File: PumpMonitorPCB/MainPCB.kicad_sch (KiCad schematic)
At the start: 2 parts, among them J1 Mains terminals, J2 Mains terminals

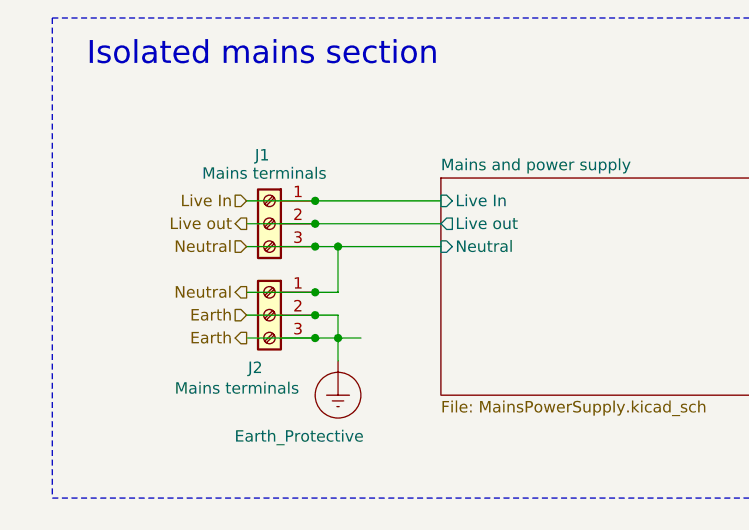
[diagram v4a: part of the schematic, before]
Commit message: Swapped current measurement to neutral (wiring diagram needs updating).
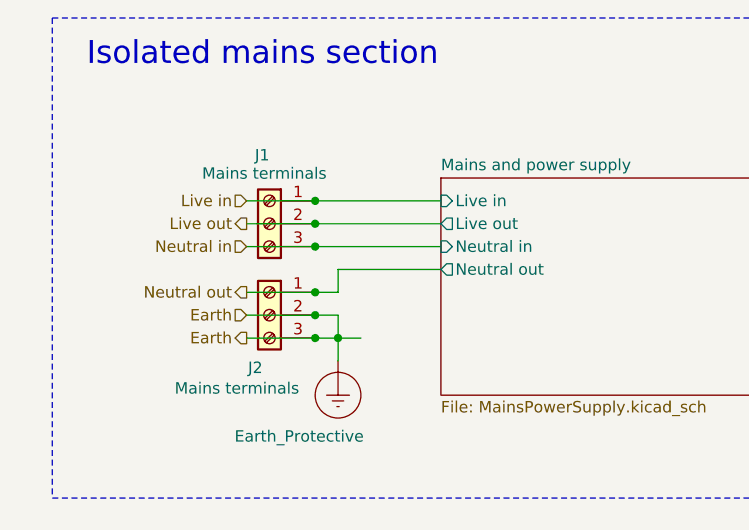
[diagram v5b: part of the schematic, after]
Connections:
- net Live In renamed Live in
- net Neutral renamed Neutral in
- net Neutral in: no longer J2.1 (Pin_1)
- new net Neutral out: J2.1 (Pin_1)
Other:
- sheet Mains and power supply ports: added Live in, Neutral in, Neutral out; removed Live In, Neutral
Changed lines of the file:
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@@
-	)
-	(junction
-		(at 68.58 53.34)
-		(diameter 0)
-		(color 0 0 0 0)
 	)
 	(junction
@@
 		)
 	)
-	(wire
-		(pts
-			(xy 66.04 58.42) (xy 68.58 58.42)
-		)
-		(stroke
-			(width 0)
-			(type default)
-		)
-	)
 	(bus
 		(pts
@@
 		(pts
 			(xy 68.58 63.5) (xy 71.12 63.5)
+		)
+		(stroke
+			(width 0)
+			(type default)
+		)
+	)
+	(wire
+		(pts
+			(xy 68.58 55.88) (xy 68.58 58.42)
 		)
 		(stroke
@@
 	(wire
 		(pts
-			(xy 66.04 53.34) (xy 68.58 53.34)
+			(xy 66.04 53.34) (xy 80.01 53.34)
 		)
 		(stroke
@@
 	(wire
 		(pts
-			(xy 68.58 53.34) (xy 80.01 53.34)
-		)
-		(stroke
-			(width 0)
-			(type default)
-		)
-	)
-	(wire
-		(pts
 			(xy 153.67 59.69) (xy 181.61 59.69)
 		)
@@
 		)
 	)
+	(wire
+		(pts
+			(xy 68.58 58.42) (xy 66.04 58.42)
+		)
+		(stroke
+			(width 0)
+			(type default)
+		)
+	)
 	(bus
 		(pts
@@
 		)
 	)
-	(wire
-		(pts
-			(xy 68.58 53.34) (xy 68.58 58.42)
-		)
-		(stroke
-			(width 0)
-			(type default)
-		)
-	)
 	(bus
 		(pts
@@
 		(pts
 			(xy 66.04 60.96) (xy 68.58 60.96)
+		)
+		(stroke
+			(width 0)
+			(type default)
+		)
+	)
+	(wire
+		(pts
+			(xy 80.01 55.88) (xy 68.58 55.88)
 		)
 		(stroke
@@
 		)
 	)
-	(hierarchical_label "Live In"
+	(hierarchical_label "Live in"
 		(shape input)
 		(at 58.42 48.26 180)
@@
 		)
 	)
-	(hierarchical_label "Neutral"
+	(hierarchical_label "Neutral out"
 		(shape output)
 		(at 58.42 58.42 180)
@@
 		)
 	)
-	(hierarchical_label "Neutral"
+	(hierarchical_label "Neutral in"
 		(shape input)
 		(at 58.42 53.34 180)
@@
 			)
 		)
-		(pin "Live In" input
+		(pin "Live in" input
 			(at 80.01 48.26 180)
-			(effects
-				(font
-					(size 1.27 1.27)
-				)
-				(justify left)
-			)
-		)
-		(pin "Neutral" input
-			(at 80.01 53.34 180)
 			(effects
 				(font
@@
 			)
 		)
+		(pin "Neutral in" input
+			(at 80.01 53.34 180)
+			(effects
+				(font
+					(size 1.27 1.27)
+				)
+				(justify left)
+			)
+		)
+		(pin "Neutral out" output
+			(at 80.01 55.88 180)
+			(effects
+				(font
+					(size 1.27 1.27)
+				)
+				(justify left)
+			)
+		)

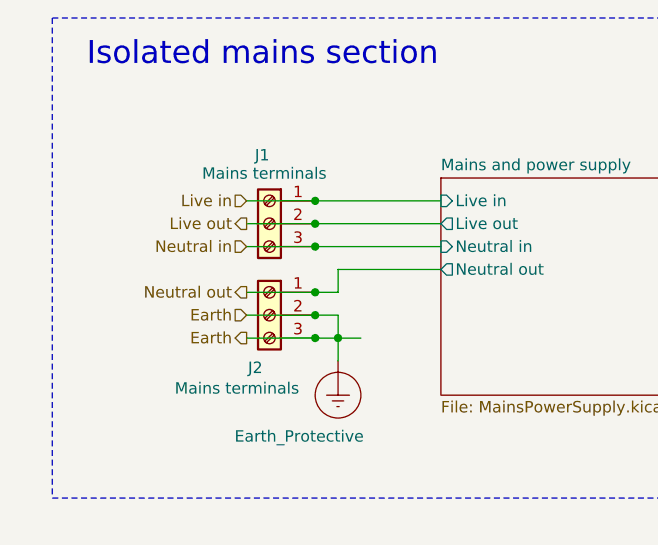
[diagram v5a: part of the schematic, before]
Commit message: Made smaller mains connector symbols, added multiple options to wiring diagram,
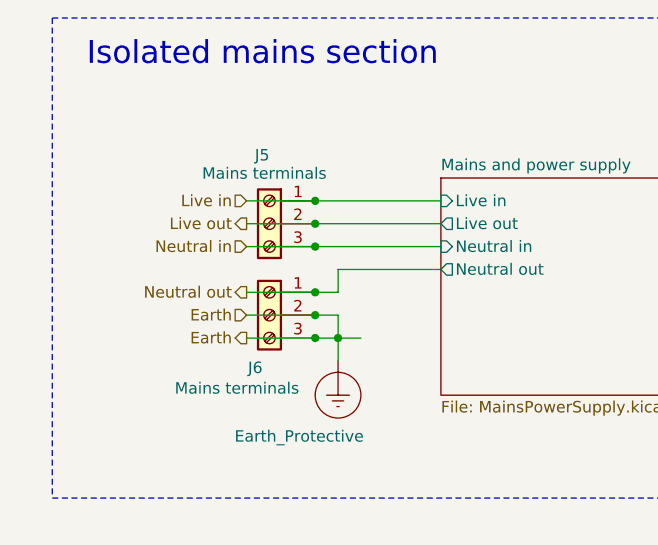
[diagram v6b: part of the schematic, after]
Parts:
- renumbered J1 to J5, J2 to J6
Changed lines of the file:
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@@
 		(on_board yes)
 		(dnp no)
-		(property "Reference" "J1"
+		(property "Reference" "J5"
 			(at 60.96 43.18 0)
 			(effects
@@
 		)
 		(pin "2"
-		)
-		(instances
-			(project ""
-				(path "/c90c4964-ca1b-44d9-8ea9-8989903af0f2/519408a1-89cc-4bd2-9b7b-cb03d2ff4d33"
-					(reference "J1")
-					(unit 1)
-				)
-			)
 		)
 	)
@@
 		(on_board yes)
 		(dnp no)
-		(property "Reference" "J2"
+		(property "Reference" "J6"
 			(at 60.198 66.802 0)
 			(effects
@@
 		(pin "2"
 		)
-		(instances
-			(project ""
-				(path "/c90c4964-ca1b-44d9-8ea9-8989903af0f2/519408a1-89cc-4bd2-9b7b-cb03d2ff4d33"
-					(reference "J2")
-					(unit 1)
-				)
-			)
-		)
 	)

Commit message: Added terminals footprint and 3D model.
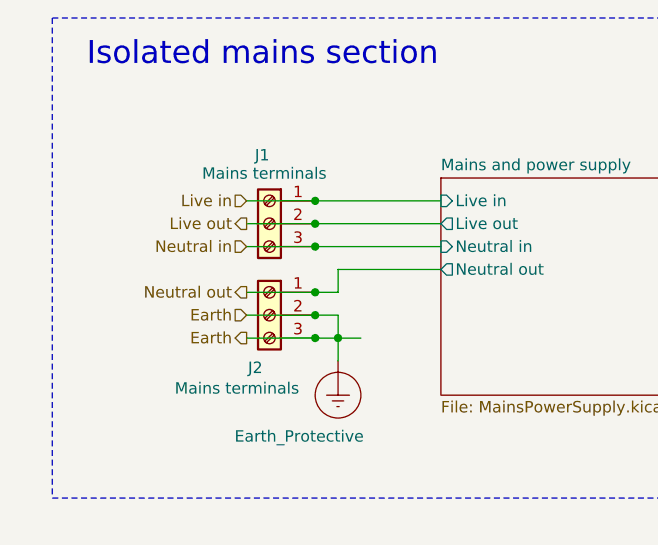
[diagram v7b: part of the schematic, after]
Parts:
- J1: renamed from J5; footprint (none) -> PumpMonitorCustomFootprints:8.25mm_ScrewTerminals
- J2: renamed from J6; footprint (none) -> PumpMonitorCustomFootprints:8.25mm_ScrewTerminals
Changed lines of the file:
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@@
 		(on_board yes)
 		(dnp no)
-		(property "Reference" "J5"
+		(property "Reference" "J1"
 			(at 60.96 43.18 0)
 			(effects
@@
 			)
 		)
-		(property "Footprint" ""
+		(property "Footprint" "PumpMonitorCustomFootprints:8.25mm_ScrewTerminals"
 			(at 60.96 50.8 0)
 			(effects
@@
 		)
 		(pin "2"
+		)
+		(instances
+			(project "PumpMonitorPCB"
+				(path "/c90c4964-ca1b-44d9-8ea9-8989903af0f2/519408a1-89cc-4bd2-9b7b-cb03d2ff4d33"
+					(reference "J1")
+					(unit 1)
+				)
+			)
 		)
 	)
@@
 		(on_board yes)
 		(dnp no)
-		(property "Reference" "J6"
+		(property "Reference" "J2"
 			(at 60.198 66.802 0)
 			(effects
@@
 			)
 		)
-		(property "Footprint" ""
+		(property "Footprint" "PumpMonitorCustomFootprints:8.25mm_ScrewTerminals"
 			(at 60.96 60.96 0)
 			(effects
@@
 		(pin "2"
 		)
+		(instances
+			(project "PumpMonitorPCB"
+				(path "/c90c4964-ca1b-44d9-8ea9-8989903af0f2/519408a1-89cc-4bd2-9b7b-cb03d2ff4d33"
+					(reference "J2")
+					(unit 1)
+				)
+			)
+		)
 	)

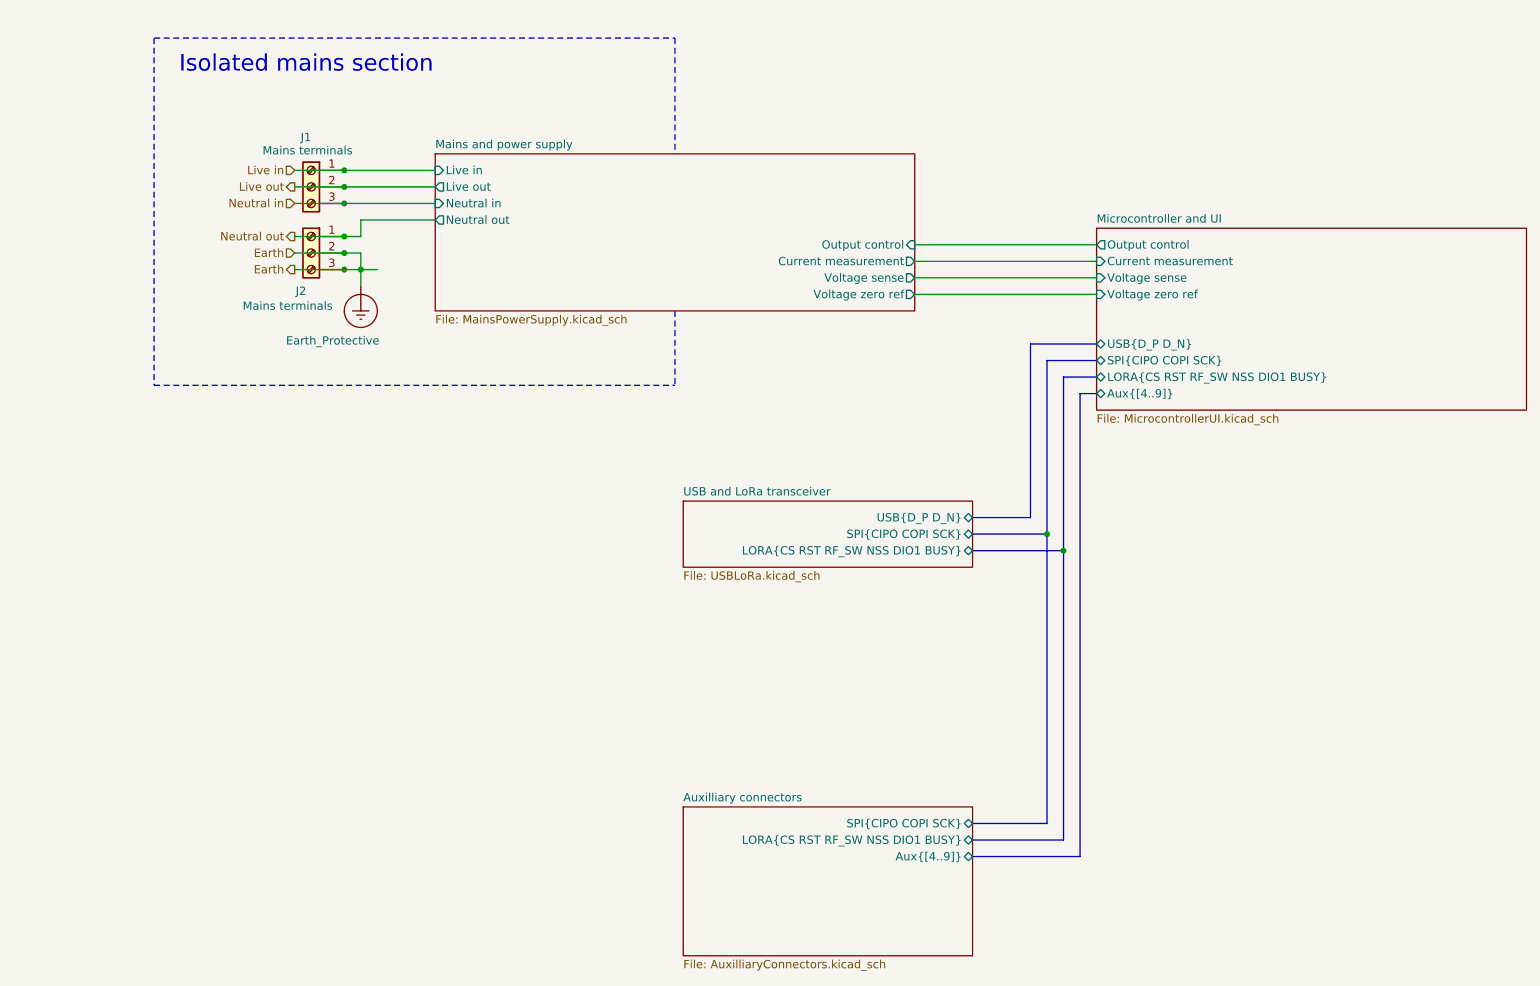
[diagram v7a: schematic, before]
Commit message: Rejigged auxilliary connectors, experimetning with kiclearance.
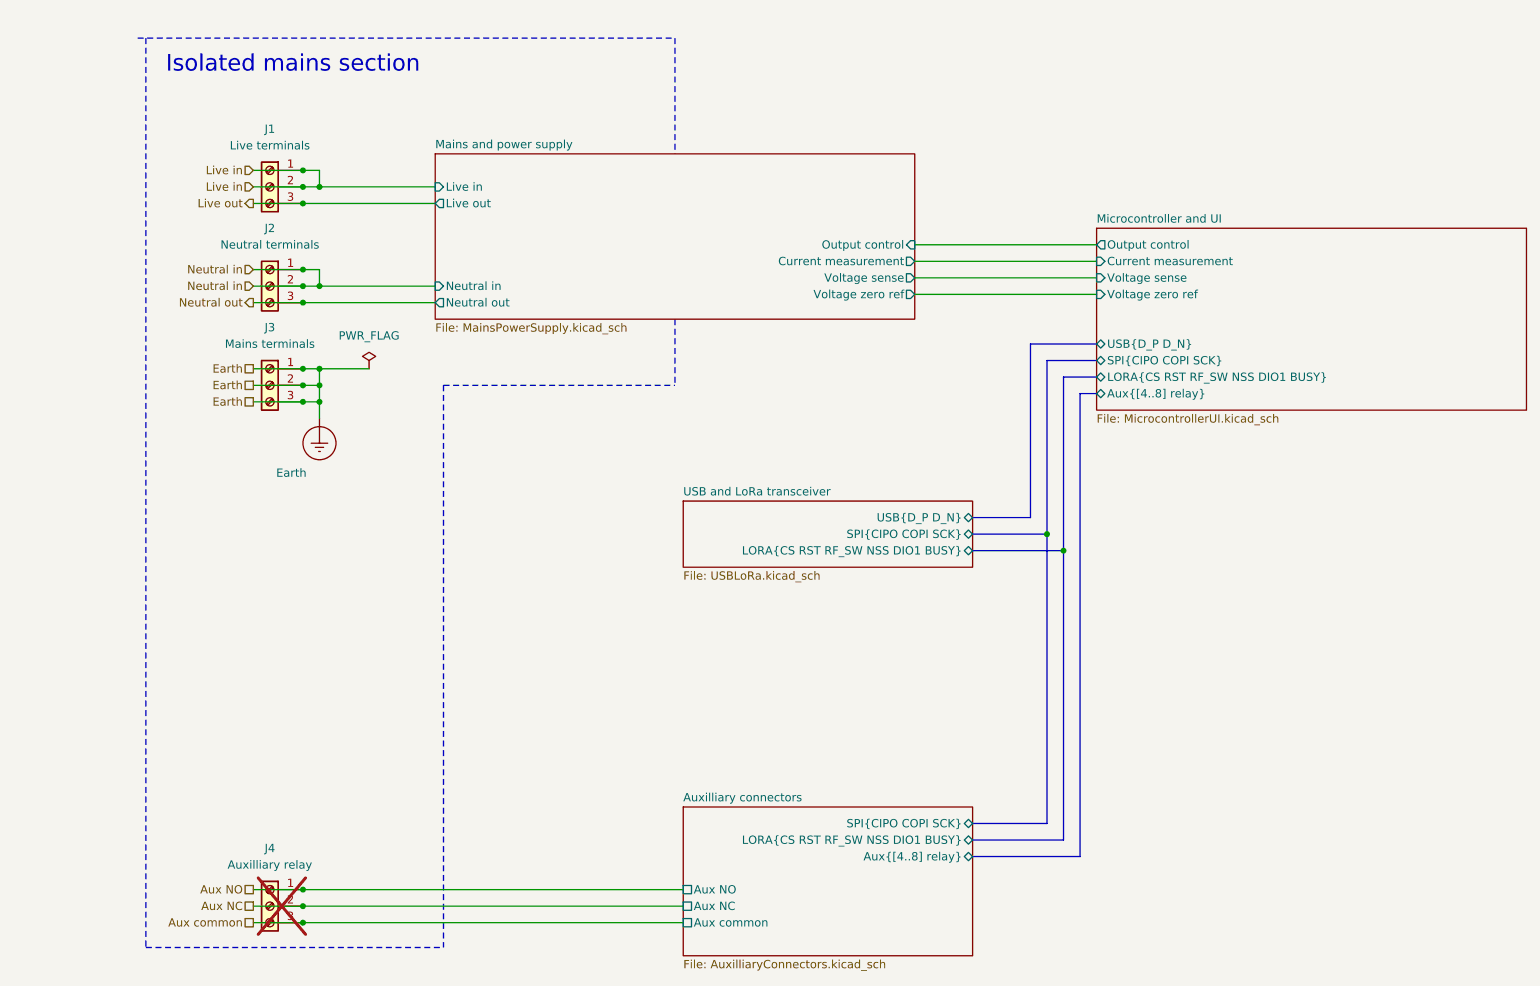
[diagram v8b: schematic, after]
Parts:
- added J3: Mains terminals, PumpMonitorCustomFootprints:8.25mm_ScrewTerminals, symbol Connector:Screw_Terminal_01x03
- added J4: Auxilliary relay, PumpMonitorCustomFootprints:8.25mm_ScrewTerminals, symbol Connector:Screw_Terminal_01x03
- J1: value Mains terminals -> Live terminals
- J2: value Mains terminals -> Neutral terminals
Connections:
- net Live in: now also J1.2 (Pin_2)
- net Live out: now also J1.3 (Pin_3); no longer J1.2 (Pin_2)
- net Neutral in: now also J2.1 (Pin_1), J2.2 (Pin_2); no longer J1.3 (Pin_3)
- net Neutral out: now also J2.3 (Pin_3); no longer J2.1 (Pin_1)
- removed net Earth_Protective: J2.2 (Pin_2), J2.3 (Pin_3)
- new net Aux NC: J4.2 (Pin_2)
- new net Aux NO: J4.1 (Pin_1)
- new net Aux common: J4.3 (Pin_3)
- new net Earth: J3.1 (Pin_1), J3.2 (Pin_2), J3.3 (Pin_3)
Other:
- sheet Auxilliary connectors ports: added Aux NC, Aux NO, Aux common, Aux{[4..8] relay}; removed Aux{[4..9]}
- sheet Microcontroller and UI ports: added Aux{[4..8] relay}; removed Aux{[4..9]}
- moved on the sheet: J1, J2
